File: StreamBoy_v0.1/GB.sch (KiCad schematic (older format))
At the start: 43 parts, among them J1 GB-CART, U2 LSF0204PWR, U3 LSF0204PWR

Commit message: Bunch of stuff
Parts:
- added D3: D, Diode_SMD:D_0805_2012Metric, symbol Device:D
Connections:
- net VCC5: now also D3.1 (K); no longer J1.1 (VCC)
- new net: D3.2 (A), J1.1 (VCC)
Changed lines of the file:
@@
 Text GLabel 3250 1550 2    50   Input ~ 0
 GB_WR
-Text GLabel 3250 1350 2    50   Input ~ 0
-VCC5
 Text GLabel 3250 1450 2    50   Input ~ 0
 GB_CLK
@@
 Text GLabel 3850 6050 0    50   Input ~ 0
 VCC3
+$Comp
+L Device:D D3
+U 1 1 5E09B24F
+P 3400 1350
+F 0 "D3" H 3400 1134 50  0000 C CNN
+F 1 "D" H 3400 1225 50  0000 C CNN
+F 2 "Diode_SMD:D_0805_2012Metric" H 3400 1350 50  0001 C CNN
+F 3 "~" H 3400 1350 50  0001 C CNN
+	1    3400 1350
+	-1   0    0    1
+$EndComp
+Text GLabel 3550 1350 2    50   Input ~ 0
+VCC5
 $EndSCHEMATC

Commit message: Power to the masses
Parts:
- removed D3: D, Diode_SMD:D_0805_2012Metric, symbol Device:D
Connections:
- net GB_5V: now reaches J1.1 (VCC)
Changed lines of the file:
@@
 Text GLabel 3850 6050 0    50   Input ~ 0
 VCC3
-$Comp
-L Device:D D3
-U 1 1 5E09B24F
-P 3400 1350
-F 0 "D3" H 3400 1134 50  0000 C CNN
-F 1 "D" H 3400 1225 50  0000 C CNN
-F 2 "Diode_SMD:D_0805_2012Metric" H 3400 1350 50  0001 C CNN
-F 3 "~" H 3400 1350 50  0001 C CNN
-	1    3400 1350
-	-1   0    0    1
-$EndComp
-Text GLabel 3550 1350 2    50   Input ~ 0
-VCC5
+Text GLabel 3250 1350 2    50   Input ~ 0
+GB_5V
 $EndSCHEMATC

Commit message: Temp
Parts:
- removed R10, R12, R14, R16, R18, R2, R20, R22, R24, R26, R28, R30, R32, R34, R36, R38, R4, R40, R6, R8: 10K, Resistor_SMD:R_0805_2012Metric, symbol Device:R
- removed R11, R13, R15, R17, R19, R21, R23, R25, R27, R29, R3, R31, R33, R35, R37, R39, R41, R5, R7, R9: 20K, Resistor_SMD:R_0805_2012Metric, symbol Device:R
- added U? (x5): LSF0204PWR, LSF0204PWR:SOP65P640X120-14N, symbol LSF0204PWR:LSF0204PWR
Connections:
- net A0: now also U?.2 (A1)
- net A1: now also U?.3 (A2)
- net A10: now also U?.4 (A3)
- net A11: now also U?.5 (A4)
- net A12: now also U?.2 (A1)
- net A13: now also U?.3 (A2)
- net A14: now also U?.4 (A3)
- net A15: now also U?.5 (A4)
- net A2: now also U?.4 (A3)
- net A3: now also U?.5 (A4)
- net A4: now also U?.2 (A1)
- net A5: now also U?.3 (A2)
- net A6: now also U?.4 (A3)
- net A7: now also U?.5 (A4)
- net A8: now also U?.2 (A1)
- net A9: now also U?.3 (A2)
- net CLK: now also U?.2 (A1)
- net CS: now also U?.5 (A4)
- net GB_A0: now also U?.13 (B1)
- net GB_A1: now also U?.12 (B2)
- net GB_A10: now also U?.11 (B3)
- net GB_A11: now also U?.10 (B4)
- net GB_A12: now also U?.13 (B1)
- net GB_A13: now also U?.12 (B2)
- net GB_A14: now also U?.11 (B3)
- net GB_A15: now also U?.10 (B4)
- net GB_A2: now also U?.11 (B3)
- net GB_A3: now also U?.10 (B4)
- net GB_A4: now also U?.13 (B1)
- net GB_A5: now also U?.12 (B2)
- net GB_A6: now also U?.11 (B3)
- net GB_A7: now also U?.10 (B4)
- net GB_A8: now also U?.13 (B1)
- net GB_A9: now also U?.12 (B2)
- net GB_CLK: now also U?.13 (B1)
- net GB_CS: now also U?.10 (B4)
- net GB_RD: now also U?.11 (B3)
- net GB_WR: now also U?.12 (B2)
- net GND: now also U?.7 (GND), U?.7 (GND), U?.7 (GND), U?.7 (GND), U?.7 (GND)
- net RD: now also U?.4 (A3)
- net VCC3: now also U?.1 (VREF_A), U?.1 (VREF_A), U?.1 (VREF_A), U?.1 (VREF_A), U?.1 (VREF_A), U?.8 (EN), U?.8 (EN), U?.8 (EN), U?.8 (EN), U?.8 (EN)
- net VCC5: now also U?.14 (VREF_B), U?.14 (VREF_B), U?.14 (VREF_B), U?.14 (VREF_B), U?.14 (VREF_B)
- net WR: now also U?.3 (A2)
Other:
- moved on the sheet: U2, U3

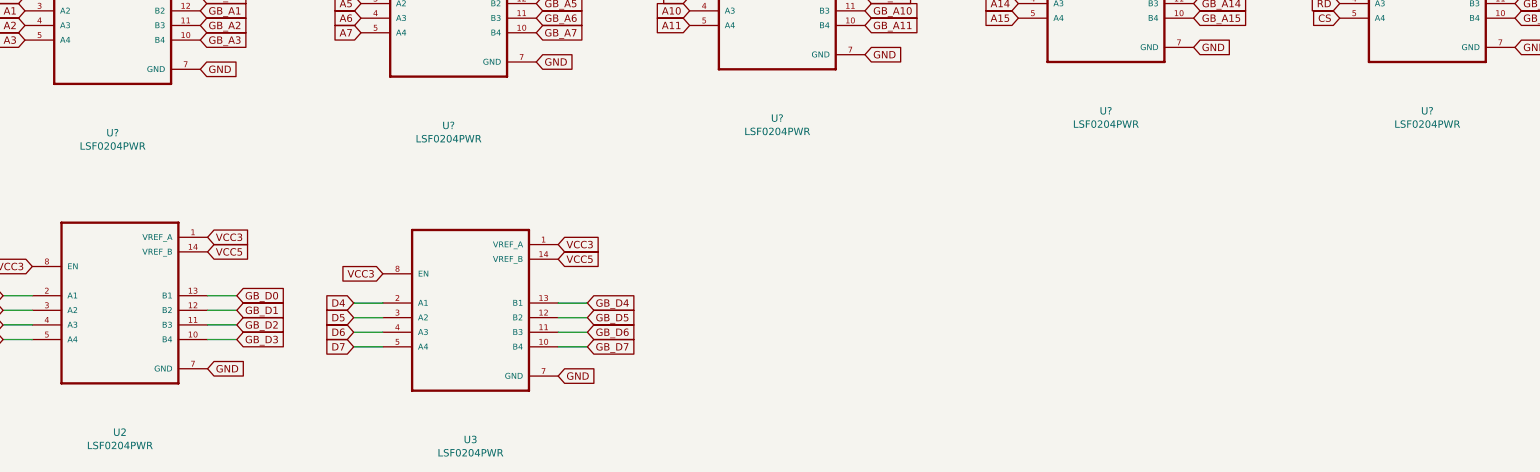
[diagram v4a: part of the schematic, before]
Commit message: Update some labels
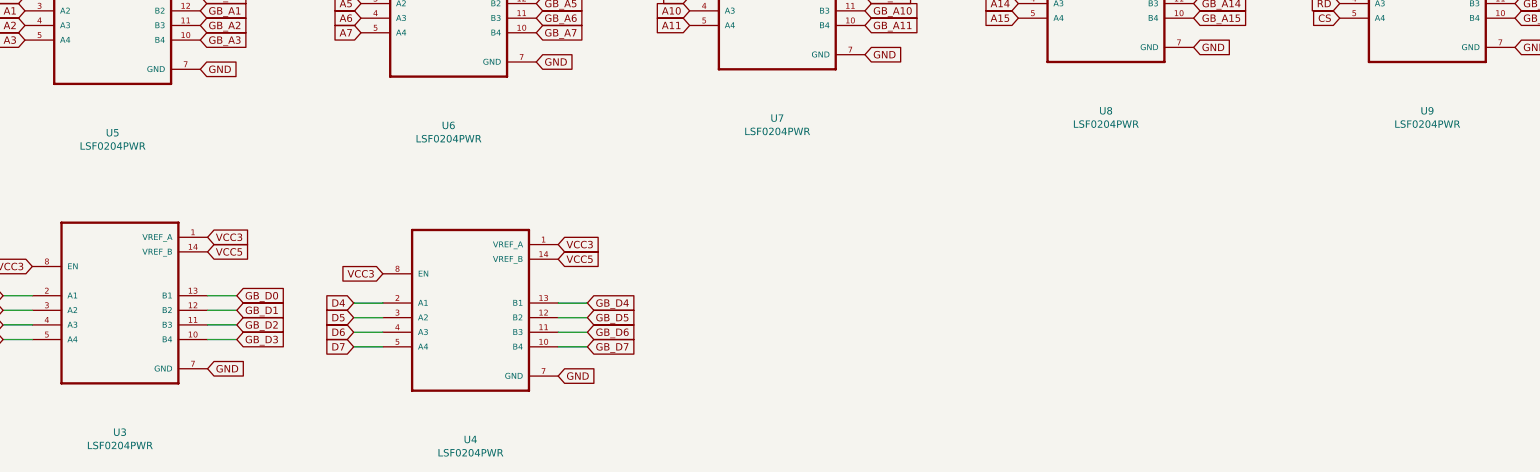
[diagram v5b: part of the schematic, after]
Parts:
- gave numbers to parts that had none: 5
- renumbered U2 to U3, U3 to U4
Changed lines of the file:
@@
 VCC3
 $Comp
-L LSF0204PWR:LSF0204PWR U3
+L LSF0204PWR:LSF0204PWR U4
 U 1 1 5E177EC5
 P 4800 8250
-F 0 "U3" H 4800 7414 50  0000 C CNN
+F 0 "U4" H 4800 7414 50  0000 C CNN
 F 1 "LSF0204PWR" H 4800 7323 50  0000 C CNN
 F 2 "LSF0204PWR:SOP65P640X120-14N" H 4800 8250 50  0001 C CNN
@@
 	1    0    0    -1
 $EndComp
-$Comp
-L LSF0204PWR:LSF0204PWR U2
-U 1 1 5E177ECB
-P 2400 8200
-F 0 "U2" H 2400 7364 50  0000 C CNN
-F 1 "LSF0204PWR" H 2400 7273 50  0000 C CNN
-F 2 "LSF0204PWR:SOP65P640X120-14N" H 2400 8200 50  0001 C CNN
-F 3 "" H 2400 8200 50  0001 C CNN
-	1    2400 8200
-	1    0    0    -1
-$EndComp
 Text GLabel 1800 7900 0    50   Input ~ 0
 VCC3
@@
 GB_5V
 $Comp
-L LSF0204PWR:LSF0204PWR U?
+L LSF0204PWR:LSF0204PWR U5
 U 1 1 5E0A2C83
 P 2350 6150
-F 0 "U?" H 2350 5314 50  0000 C CNN
+F 0 "U5" H 2350 5314 50  0000 C CNN
 F 1 "LSF0204PWR" H 2350 5223 50  0000 C CNN
 F 2 "LSF0204PWR:SOP65P640X120-14N" H 2350 6150 50  0001 C CNN
@@
 $EndComp
 $Comp
-L LSF0204PWR:LSF0204PWR U?
+L LSF0204PWR:LSF0204PWR U6
 U 1 1 5E0A3A1F
 P 4650 6100
-F 0 "U?" H 4650 5264 50  0000 C CNN
+F 0 "U6" H 4650 5264 50  0000 C CNN
 F 1 "LSF0204PWR" H 4650 5173 50  0000 C CNN
 F 2 "LSF0204PWR:SOP65P640X120-14N" H 4650 6100 50  0001 C CNN
@@
 $EndComp
 $Comp
-L LSF0204PWR:LSF0204PWR U?
+L LSF0204PWR:LSF0204PWR U7
 U 1 1 5E0A417D
 P 6900 6050
-F 0 "U?" H 6900 5214 50  0000 C CNN
+F 0 "U7" H 6900 5214 50  0000 C CNN
 F 1 "LSF0204PWR" H 6900 5123 50  0000 C CNN
 F 2 "LSF0204PWR:SOP65P640X120-14N" H 6900 6050 50  0001 C CNN
@@
 $EndComp
 $Comp
-L LSF0204PWR:LSF0204PWR U?
+L LSF0204PWR:LSF0204PWR U8
 U 1 1 5E0A490A
 P 9150 6000
-F 0 "U?" H 9150 5164 50  0000 C CNN
+F 0 "U8" H 9150 5164 50  0000 C CNN
 F 1 "LSF0204PWR" H 9150 5073 50  0000 C CNN
 F 2 "LSF0204PWR:SOP65P640X120-14N" H 9150 6000 50  0001 C CNN
@@
 $EndComp
 $Comp
-L LSF0204PWR:LSF0204PWR U?
+L LSF0204PWR:LSF0204PWR U9
 U 1 1 5E0BAF3B
 P 11350 6000
-F 0 "U?" H 11350 5164 50  0000 C CNN
+F 0 "U9" H 11350 5164 50  0000 C CNN
 F 1 "LSF0204PWR" H 11350 5073 50  0000 C CNN
 F 2 "LSF0204PWR:SOP65P640X120-14N" H 11350 6000 50  0001 C CNN
@@
 Text GLabel 8550 6200 0    50   Input ~ 0
 A15
+$Comp
+L LSF0204PWR:LSF0204PWR U3
+U 1 1 5E177ECB
+P 2400 8200
+F 0 "U3" H 2400 7364 50  0000 C CNN
+F 1 "LSF0204PWR" H 2400 7273 50  0000 C CNN
+F 2 "LSF0204PWR:SOP65P640X120-14N" H 2400 8200 50  0001 C CNN
+F 3 "" H 2400 8200 50  0001 C CNN
+	1    2400 8200
+	1    0    0    -1
+$EndComp
 $EndSCHEMATC

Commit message: More renumbering
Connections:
- net A0: now also U5.5 (A4); no longer U5.2 (A1)
- net A1: now also U5.4 (A3); no longer U5.3 (A2)
- net A10: now also U7.3 (A2); no longer U7.4 (A3)
- net A11: now also U7.2 (A1); no longer U7.5 (A4)
- net A12: now also U8.5 (A4); no longer U8.2 (A1)
- net A13: now also U8.4 (A3); no longer U8.3 (A2)
- net A14: now also U8.3 (A2); no longer U8.4 (A3)
- net A15: now also U8.2 (A1); no longer U8.5 (A4)
- net A2: now also U5.3 (A2); no longer U5.4 (A3)
- net A3: now also U5.2 (A1); no longer U5.5 (A4)
- net A4: now also U6.5 (A4); no longer U6.2 (A1)
- net A5: now also U6.4 (A3); no longer U6.3 (A2)
- net A6: now also U6.3 (A2); no longer U6.4 (A3)
- net A7: now also U6.2 (A1); no longer U6.5 (A4)
- net A8: now also U7.5 (A4); no longer U7.2 (A1)
- net A9: now also U7.4 (A3); no longer U7.3 (A2)
- net CLK: now also U9.5 (A4); no longer U9.2 (A1)
- net CS: now also U9.2 (A1); no longer U9.5 (A4)
- net D0: now also U3.5 (A4); no longer U3.2 (A1)
- net D1: now also U3.4 (A3); no longer U3.3 (A2)
- net D2: now also U3.3 (A2); no longer U3.4 (A3)
- net D3: now also U3.2 (A1); no longer U3.5 (A4)
- net D4: now also U4.5 (A4); no longer U4.2 (A1)
- net D5: now also U4.4 (A3); no longer U4.3 (A2)
- net D6: now also U4.3 (A2); no longer U4.4 (A3)
- net D7: now also U4.2 (A1); no longer U4.5 (A4)
- net GB_A0: now also U5.10 (B4); no longer U5.13 (B1)
- net GB_A1: now also U5.11 (B3); no longer U5.12 (B2)
- net GB_A10: now also U7.12 (B2); no longer U7.11 (B3)
- net GB_A11: now also U7.13 (B1); no longer U7.10 (B4)
- net GB_A12: now also U8.10 (B4); no longer U8.13 (B1)
- net GB_A13: now also U8.11 (B3); no longer U8.12 (B2)
- net GB_A14: now also U8.12 (B2); no longer U8.11 (B3)
- net GB_A15: now also U8.13 (B1); no longer U8.10 (B4)
- net GB_A2: now also U5.12 (B2); no longer U5.11 (B3)
- net GB_A3: now also U5.13 (B1); no longer U5.10 (B4)
- net GB_A4: now also U6.10 (B4); no longer U6.13 (B1)
- net GB_A5: now also U6.11 (B3); no longer U6.12 (B2)
- net GB_A6: now also U6.12 (B2); no longer U6.11 (B3)
- net GB_A7: now also U6.13 (B1); no longer U6.10 (B4)
- net GB_A8: now also U7.10 (B4); no longer U7.13 (B1)
- net GB_A9: now also U7.11 (B3); no longer U7.12 (B2)
- net GB_CLK: now also U9.10 (B4); no longer U9.13 (B1)
- net GB_CS: now also U9.13 (B1); no longer U9.10 (B4)
- net GB_D0: now also U3.10 (B4); no longer U3.13 (B1)
- net GB_D1: now also U3.11 (B3); no longer U3.12 (B2)
- net GB_D2: now also U3.12 (B2); no longer U3.11 (B3)
- net GB_D3: now also U3.13 (B1); no longer U3.10 (B4)
- net GB_D4: now also U4.10 (B4); no longer U4.13 (B1)
- net GB_D5: now also U4.11 (B3); no longer U4.12 (B2)
- net GB_D6: now also U4.12 (B2); no longer U4.11 (B3)
- net GB_D7: now also U4.13 (B1); no longer U4.10 (B4)
- net GB_RD: now also U9.12 (B2); no longer U9.11 (B3)
- net GB_WR: now also U9.11 (B3); no longer U9.12 (B2)
- net RD: now also U9.3 (A2); no longer U9.4 (A3)
- net WR: now also U9.4 (A3); no longer U9.3 (A2)

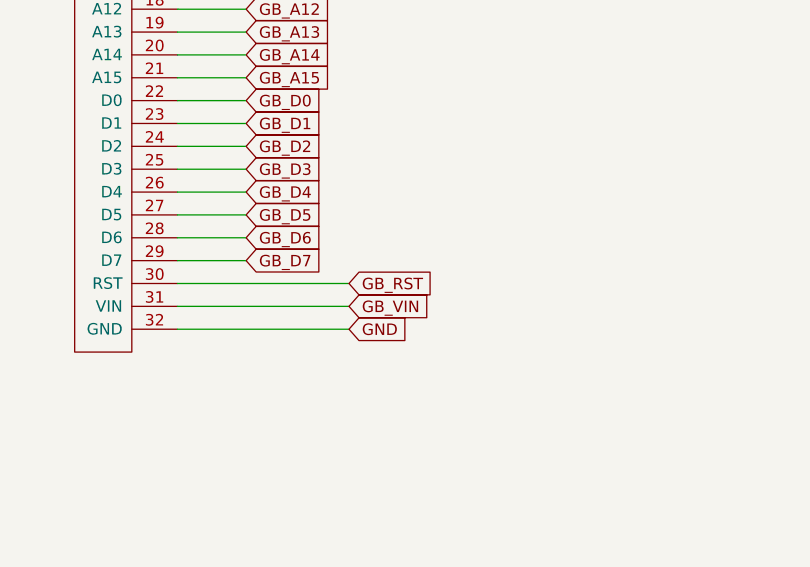
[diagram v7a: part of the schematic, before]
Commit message: GB Reset fixed and moved some stuff
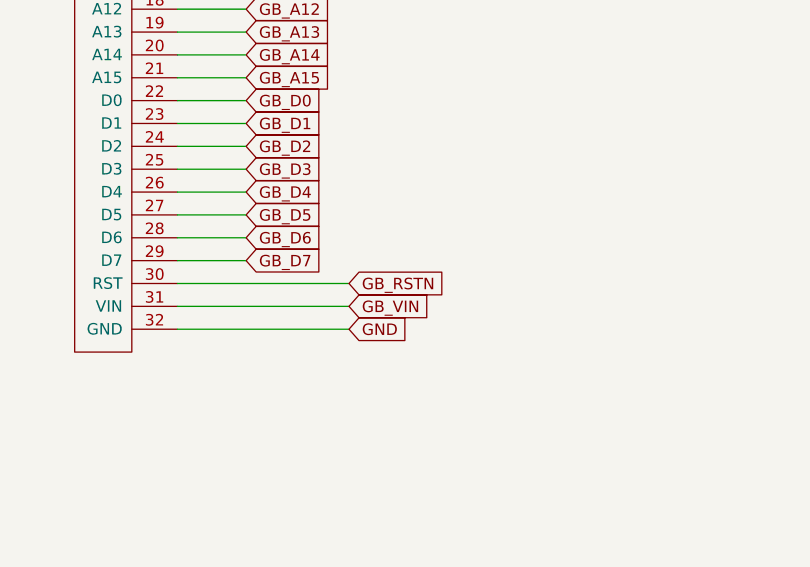
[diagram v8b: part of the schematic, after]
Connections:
- net GB_RST renamed GB_RSTN
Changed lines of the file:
@@
 GB_CS
 Text GLabel 3250 4250 2    50   Input ~ 0
-GB_RST
+GB_RSTN
 Text GLabel 3250 4350 2    50   Input ~ 0
 GB_VIN
